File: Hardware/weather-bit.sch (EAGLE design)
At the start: 41 parts, among them J1 EDGE-80PTH-RA, J2 RJ11, J3 RJ11, U1 BME280

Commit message: Updated brd and sch file 3/28/2017
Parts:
- removed R2, R3: 4.7k, SparkFun-Resistors:4.7KOHM-0603-1/10W-1%
- added I2C: JUMPER-SMT_3_2-NC_TRACE_SILK, SparkFun-Jumpers:JUMPER-SMT_3_2-NC_TRACE_SILK
- added J8, J9: (no value), SparkFun-Connectors:CONN_04
- added R12, R13: 4.7k, SparkFun-Resistors:4.7KOHM-0603-1/10W-1%
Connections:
- removed net 14: J1.A17
- removed net 15: J1.A16
- new net N$4: I2C.3, R12.2
- new net N$8: I2C.1, R13.2
- new net RXI: J1.A17, J8.2
- new net TXO: J1.A16, J8.1
- net 3.3V: now also I2C.2, J8.4, J9.3; no longer R2.2, R3.2
- net GND: now also J8.3, J9.4
- net SCL: now also J9.1, R13.1; no longer R3.1
- net SDA: now also J9.2, R12.1; no longer R2.1
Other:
- note added: "I2C Port"
- note added: "RXI"
- note added: "Serial Port"
- note added: "TXO"

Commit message: updated board and sch files 3/29
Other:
- note added: "Mary West, based on Weather Shield design by Nathan Seidle"
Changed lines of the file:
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@@
 <text x="66.04" y="60.96" size="2.54" layer="97" font="vector">I2C Port </text>
 <wire x1="58.42" y1="68.58" x2="58.42" y2="0" width="0.1524" layer="97" style="longdash"/>
+<text x="167.64" y="10.16" size="1.778" layer="94">Mary West, based on Weather Shield design by Nathan Seidle</text>
 </plain>
 <instances>

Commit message: Adding Library Part Updated Brd File Updated Sch File 3/30/2017
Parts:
- removed I2C: JUMPER-SMT_3_2-NC_TRACE_SILK, SparkFun-Jumpers:JUMPER-SMT_3_2-NC_TRACE_SILK
- removed J1: EDGE-80PTH-RA, local_lib:EDGE-80PTH-RA
- removed R12, R13: 4.7k, SparkFun-Resistors:4.7KOHM-0603-1/10W-1%
- added U2: micro:bit, Micro_Bit_Parts:MICRO:BITLEDS_UP
- LOGO2: value SFE_LOGO_NAME_FLAME.1_INCH -> SFE_LOGO_NAME_FLAME.3_INCH; device SparkFun-Aesthetics:SFE_LOGO_NAME_FLAME.1_INCH -> SparkFun-Aesthetics:SFE_LOGO_NAME_FLAME.3_INCH
- LOGO3, LOGO4: value OSHW-LOGOS -> OSHW-LOGOL; device SparkFun-Aesthetics:OSHW-LOGOS -> SparkFun-Aesthetics:OSHW-LOGOL
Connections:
- removed net N$4: I2C.3, R12.2
- removed net N$8: I2C.1, R13.2
- net 10: now also U2.P10; no longer J1.A25
- net 11: now also U2.P11; no longer J1.A24
- net 13: now also U2.P13; no longer J1.A18
- net 3: now also U2.P3; no longer J1.A40
- net 3.3V: now also U2.3.3V; no longer I2C.2, J1.A10, J1.A11, J1.A12, J1.A13, J1.A14, J1.A9
- net 4: now also U2.P4; no longer J1.A35
- net 5: now also U2.P5; no longer J1.A34
- net 6: now also U2.P6; no longer J1.A33
- net 7: now also U2.P7; no longer J1.A32
- net 9: now also U2.P9; no longer J1.A26
- net GND: now also U2.GND; no longer J1.A1, J1.A2, J1.A3, J1.A4, J1.A5, J1.A6
- net RAIN: now also U2.P2; no longer J1.A19, J1.A20, J1.A21, J1.A22
- net RXI: now also U2.P14; no longer J1.A17
- net SCL: now also U2.P19; no longer J1.A8, R13.1
- net SDA: now also U2.P20; no longer J1.A7, R12.1
- net SOIL_DAT: now also U2.P0; no longer J1.A36, J1.A37, J1.A38, J1.A39
- net SOIL_PWR: now also U2.P16; no longer J1.A15
- net TEMP_DAT: now also U2.P12; no longer J1.A23
- net TXO: now also U2.P15; no longer J1.A16
- net WDIR: now also U2.P1; no longer J1.A28, J1.A29, J1.A30, J1.A31
- net WSPEED: now also U2.P8; no longer J1.A27

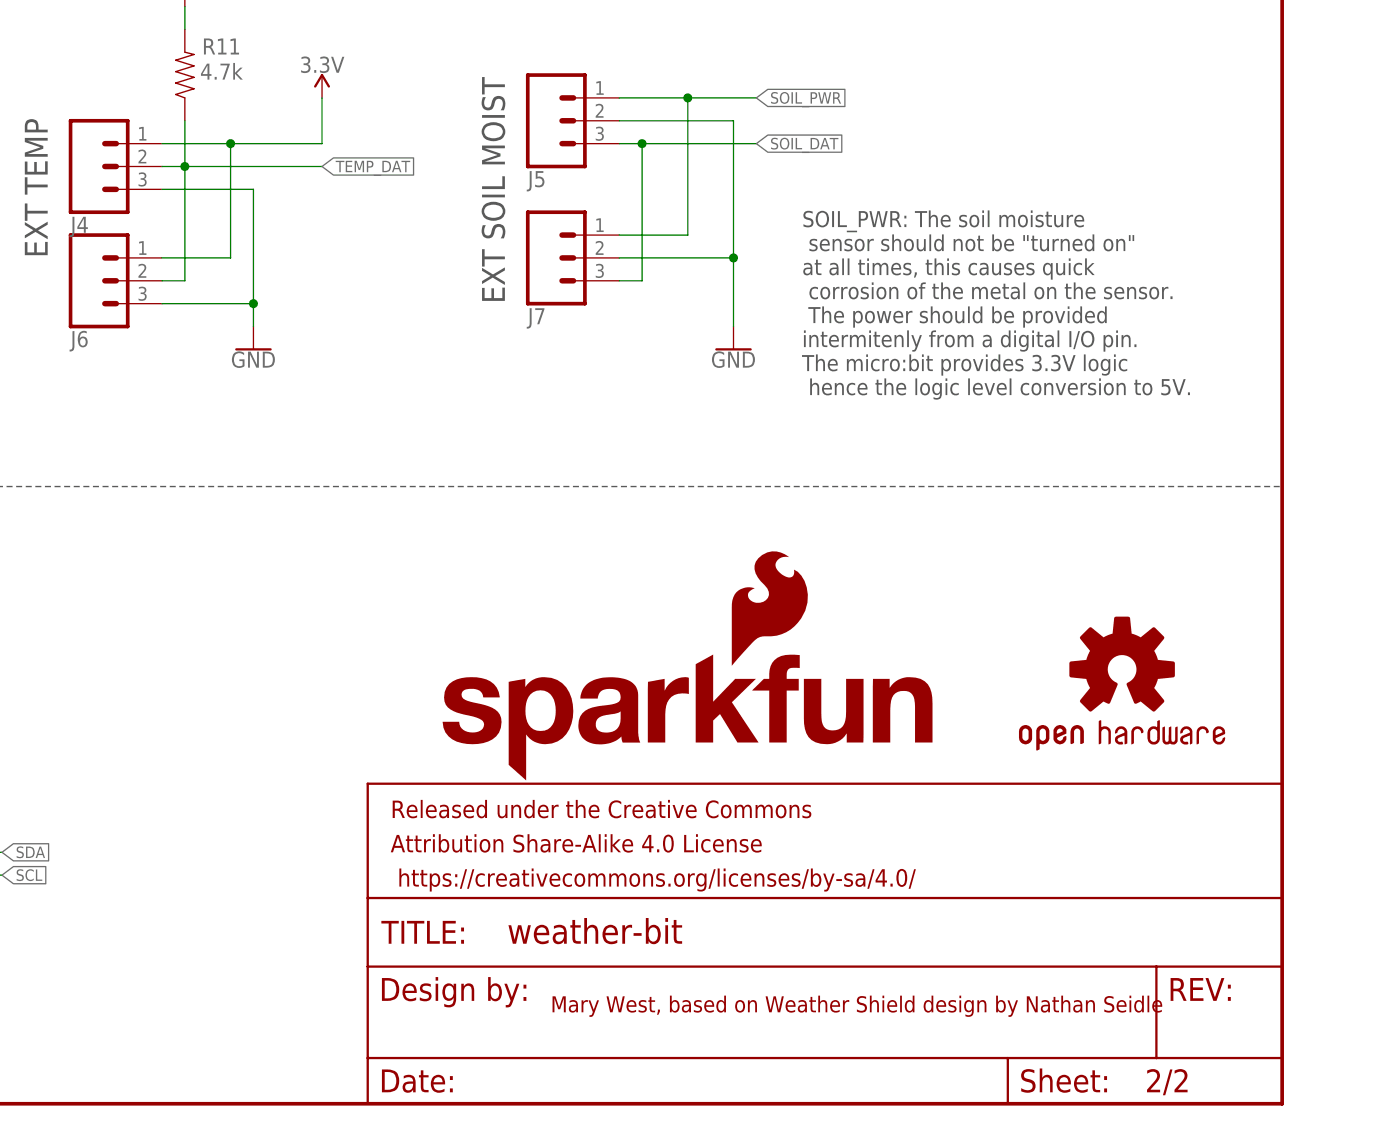
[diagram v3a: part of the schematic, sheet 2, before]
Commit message: Updated BRD and SCH files per Design Review 3/31
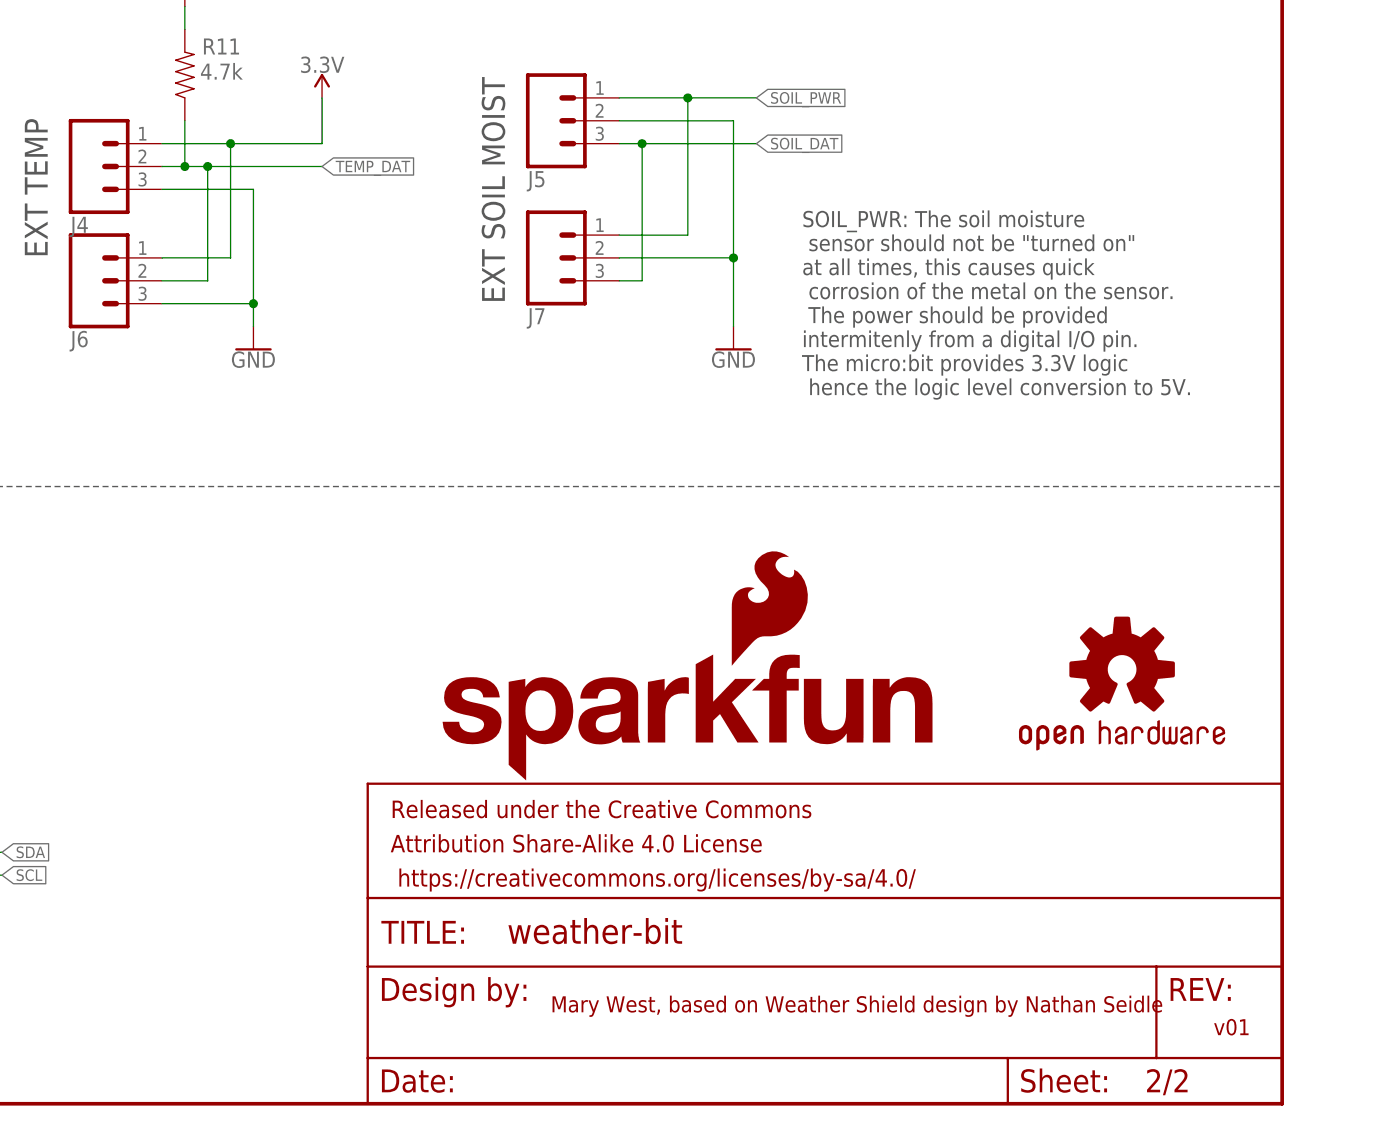
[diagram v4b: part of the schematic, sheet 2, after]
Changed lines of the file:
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@@
 The micro:bit provides 3.3V logic
  hence the logic level conversion to 5V. </text>
-<text x="111.76" y="93.98" size="2.54" layer="97" rot="R90">EXT TEMP</text>
-<text x="162.56" y="88.9" size="2.54" layer="97" rot="R90">EXT SOIL MOIST</text>
+<text x="111.76" y="93.98" size="2.54" layer="97" font="vector" rot="R90">EXT TEMP</text>
+<text x="162.56" y="88.9" size="2.54" layer="97" font="vector" rot="R90">EXT SOIL MOIST</text>
 <wire x1="96.52" y1="68.58" x2="248.92" y2="68.58" width="0.1524" layer="97" style="longdash"/>
 <wire x1="0" y1="134.62" x2="96.52" y2="134.62" width="0.1524" layer="97" style="longdash"/>
@@
 <wire x1="58.42" y1="68.58" x2="58.42" y2="0" width="0.1524" layer="97" style="longdash"/>
 <text x="167.64" y="10.16" size="1.778" layer="94">Mary West, based on Weather Shield design by Nathan Seidle</text>
+<text x="241.3" y="7.62" size="1.778" layer="94">v01</text>
 </plain>
 <instances>
@@
 <pinref part="R11" gate="G$1" pin="1"/>
 <wire x1="127" y1="109.22" x2="127" y2="104.14" width="0.1524" layer="91"/>
-<wire x1="127" y1="104.14" x2="127" y2="91.44" width="0.1524" layer="91"/>
+<junction x="127" y="104.14"/>
+<wire x1="127" y1="104.14" x2="129.54" y2="104.14" width="0.1524" layer="91"/>
+<label x="142.24" y="104.14" size="1.27" layer="95" xref="yes"/>
 <pinref part="J6" gate="J$1" pin="2"/>
-<wire x1="127" y1="91.44" x2="124.46" y2="91.44" width="0.1524" layer="91"/>
-<junction x="127" y="104.14"/>
-<wire x1="127" y1="104.14" x2="142.24" y2="104.14" width="0.1524" layer="91"/>
-<label x="142.24" y="104.14" size="1.27" layer="95" xref="yes"/>
-</segment>
-</net>
+<wire x1="129.54" y1="104.14" x2="142.24" y2="104.14" width="0.1524" layer="91"/>
+<wire x1="124.46" y1="91.44" x2="129.54" y2="91.44" width="0.1524" layer="91"/>
+<wire x1="129.54" y1="91.44" x2="129.54" y2="104.14" width="0.1524" layer="91"/>
+<junction x="129.54" y="104.14"/>
+</segment>
+</net>

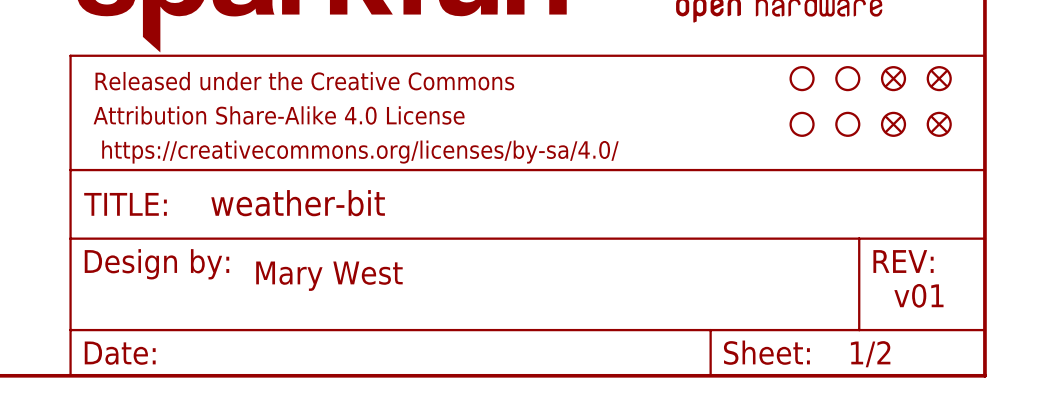
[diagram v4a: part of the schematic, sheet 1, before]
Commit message: Updated brd and sch files per QC Review
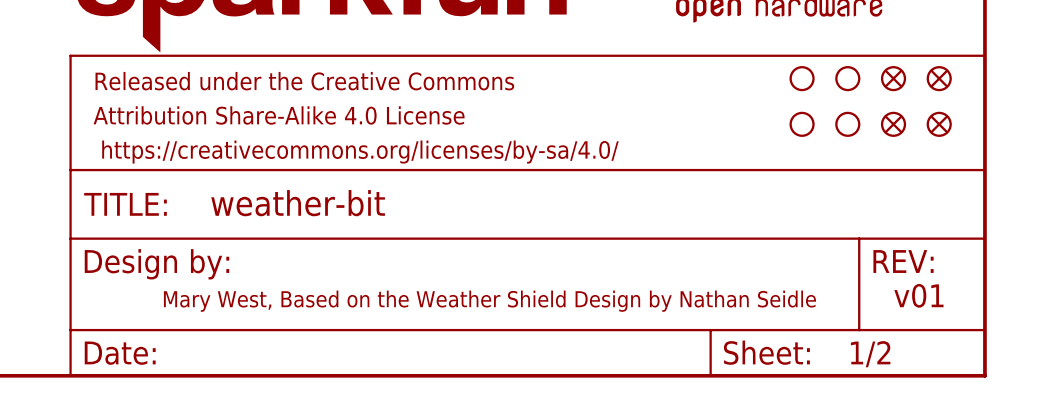
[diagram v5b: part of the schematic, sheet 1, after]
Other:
- note added: "Mary West, Based on the Weather Shield Design by Nathan Seidle"
- note removed: "Mary West"
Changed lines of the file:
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@@
 <text x="238.76" y="7.62" size="2.54" layer="94">v01</text>
 <text x="5.08" y="175.26" size="5.08" layer="97">CONNECTOR</text>
-<text x="167.64" y="10.16" size="2.54" layer="94" font="vector">Mary West </text>
 <text x="149.86" y="93.98" size="1.778" layer="97">20
 19
@@
 <text x="175.26" y="134.62" size="1.27" layer="97">TXO</text>
 <text x="175.26" y="132.08" size="1.27" layer="97">RXI</text>
+<text x="157.48" y="7.62" size="1.778" layer="94">Mary West, Based on the Weather Shield Design by Nathan Seidle</text>
 </plain>
 <instances>

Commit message: Updated BRD and SCH files per EDU
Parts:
- removed J8: (no value), SparkFun-Connectors:CONN_04
- removed LOGO4: OSHW-LOGOL, SparkFun-Aesthetics:OSHW-LOGOL
- added J1: (no value), SparkFun-Connectors:6_PIN_SERIAL_TARGETSILK
- J9: device SparkFun-Connectors:CONN_04 -> SparkFun-Connectors:CONN_041X04_NO_SILK
- LOGO1: value SFE_LOGO_NAME_FLAME.1_INCH -> SFE_LOGO_NAME_FLAME.2_INCH; device SparkFun-Aesthetics:SFE_LOGO_NAME_FLAME.1_INCH -> SparkFun-Aesthetics:SFE_LOGO_NAME_FLAME.2_INCH
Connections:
- net 3.3V: now also J1.VCC; no longer J8.4
- net GND: now also J1.CTS, J1.GND; no longer J8.3
- net RXI: now also J1.RXI; no longer J8.2
- net TXO: now also J1.TXO; no longer J8.1
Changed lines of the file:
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@@
 <part name="J7" library="SparkFun-Connectors" deviceset="CONN_03" device=""/>
 <part name="R11" library="SparkFun-Resistors" deviceset="4.7KOHM" device="-0603-1/10W-1%" value="4.7k"/>
-<part name="LOGO1" library="SparkFun-Aesthetics" deviceset="SFE_LOGO_NAME_FLAME" device=".1_INCH" value="SFE_LOGO_NAME_FLAME.1_INCH"/>
-<part name="LOGO4" library="SparkFun-Aesthetics" deviceset="OSHW-LOGO" device="L" value="OSHW-LOGOL"/>
+<part name="LOGO1" library="SparkFun-Aesthetics" deviceset="SFE_LOGO_NAME_FLAME" device=".2_INCH" value="SFE_LOGO_NAME_FLAME.2_INCH"/>
 <part name="GND15" library="SparkFun-PowerSymbols" deviceset="GND" device=""/>
 <part name="GND16" library="SparkFun-PowerSymbols" deviceset="GND" device=""/>
@@
 <part name="SUPPLY9" library="SparkFun-PowerSymbols" deviceset="3.3V" device=""/>
 <part name="SUPPLY10" library="SparkFun-PowerSymbols" deviceset="3.3V" device=""/>
-<part name="J8" library="SparkFun-Connectors" deviceset="CONN_04" device=""/>
-<part name="J9" library="SparkFun-Connectors" deviceset="CONN_04" device=""/>
+<part name="J9" library="SparkFun-Connectors" deviceset="CONN_04" device="1X04_NO_SILK"/>
 <part name="SUPPLY11" library="SparkFun-PowerSymbols" deviceset="3.3V" device=""/>
 <part name="GND2" library="SparkFun-PowerSymbols" deviceset="GND" device=""/>
@@
 <part name="SUPPLY8" library="SparkFun-PowerSymbols" deviceset="3.3V" device=""/>
 <part name="GND4" library="SparkFun-PowerSymbols" deviceset="GND" device=""/>
+<part name="J1" library="SparkFun-Connectors" deviceset="6_PIN_SERIAL_TARGET" device="SILK"/>
 </parts>
 <sheets>
@@
 </instance>
 <instance part="LOGO1" gate="G$1" x="154.94" y="35.56"/>
-<instance part="LOGO4" gate="G$1" x="231.14" y="48.26"/>
 <instance part="GND15" gate="1" x="134.62" y="83.82"/>
 <instance part="GND16" gate="1" x="187.96" y="83.82"/>
@@
 <instance part="SUPPLY9" gate="G$1" x="166.37" y="179.324"/>
 <instance part="SUPPLY10" gate="G$1" x="173.99" y="179.324"/>
-<instance part="J8" gate="G$1" x="20.32" y="38.1"/>
 <instance part="J9" gate="G$1" x="78.74" y="27.94"/>
-<instance part="SUPPLY11" gate="G$1" x="33.02" y="48.26"/>
-<instance part="GND2" gate="1" x="33.02" y="22.86"/>
+<instance part="SUPPLY11" gate="G$1" x="33.02" y="53.34"/>
+<instance part="GND2" gate="1" x="27.94" y="25.4"/>
 <instance part="SUPPLY12" gate="G$1" x="88.9" y="40.64"/>
 <instance part="GND3" gate="1" x="91.44" y="15.24"/>
+<instance part="J1" gate="G$1" x="17.78" y="40.64"/>
 </instances>
 <busses>
@@
 </segment>
 <segment>
-<pinref part="J8" gate="G$1" pin="3"/>
-<wire x1="25.4" y1="40.64" x2="33.02" y2="40.64" width="0.1524" layer="91"/>
-<wire x1="33.02" y1="40.64" x2="33.02" y2="25.4" width="0.1524" layer="91"/>
-<pinref part="GND2" gate="1" pin="GND"/>
-</segment>
-<segment>
 <pinref part="J9" gate="G$1" pin="4"/>
 <wire x1="83.82" y1="33.02" x2="91.44" y2="33.02" width="0.1524" layer="91"/>
 <wire x1="91.44" y1="33.02" x2="91.44" y2="17.78" width="0.1524" layer="91"/>
 <pinref part="GND3" gate="1" pin="GND"/>
+</segment>
+<segment>
+<pinref part="J1" gate="G$1" pin="GND"/>
+<wire x1="22.86" y1="48.26" x2="27.94" y2="48.26" width="0.1524" layer="91"/>
+<wire x1="27.94" y1="48.26" x2="27.94" y2="45.72" width="0.1524" layer="91"/>
+<pinref part="GND2" gate="1" pin="GND"/>
+<pinref part="J1" gate="G$1" pin="CTS"/>
+<wire x1="27.94" y1="45.72" x2="27.94" y2="27.94" width="0.1524" layer="91"/>
+<wire x1="22.86" y1="45.72" x2="27.94" y2="45.72" width="0.1524" layer="91"/>
+<junction x="27.94" y="45.72"/>
 </segment>
 </net>
@@
 </segment>
 <segment>
-<pinref part="J8" gate="G$1" pin="4"/>
-<wire x1="25.4" y1="43.18" x2="33.02" y2="43.18" width="0.1524" layer="91"/>
-<wire x1="33.02" y1="43.18" x2="33.02" y2="48.26" width="0.1524" layer="91"/>
-<pinref part="SUPPLY11" gate="G$1" pin="3.3V"/>
-</segment>
-<segment>
 <pinref part="J9" gate="G$1" pin="3"/>
 <wire x1="83.82" y1="30.48" x2="88.9" y2="30.48" width="0.1524" layer="91"/>
 <wire x1="88.9" y1="30.48" x2="88.9" y2="40.64" width="0.1524" layer="91"/>
 <pinref part="SUPPLY12" gate="G$1" pin="3.3V"/>
+</segment>
+<segment>
+<pinref part="J1" gate="G$1" pin="VCC"/>
+<wire x1="22.86" y1="43.18" x2="33.02" y2="43.18" width="0.1524" layer="91"/>
+<pinref part="SUPPLY11" gate="G$1" pin="3.3V"/>
+<wire x1="33.02" y1="43.18" x2="33.02" y2="53.34" width="0.1524" layer="91"/>
 </segment>
 </net>
@@
 </segment>
 </net>
+<net name="TXO" class="0">
+<segment>
+<pinref part="J1" gate="G$1" pin="TXO"/>
+<wire x1="22.86" y1="40.64" x2="35.56" y2="40.64" width="0.1524" layer="91"/>
+<label x="35.56" y="40.64" size="1.27" layer="95" font="vector" xref="yes"/>
+</segment>
+</net>
 <net name="RXI" class="0">
 <segment>
-<pinref part="J8" gate="G$1" pin="2"/>
-<wire x1="25.4" y1="38.1" x2="38.1" y2="38.1" width="0.1524" layer="91"/>
-<label x="38.1" y="38.1" size="1.27" layer="95" xref="yes"/>
-</segment>
-</net>
-<net name="TXO" class="0">
-<segment>
-<pinref part="J8" gate="G$1" pin="1"/>
-<wire x1="25.4" y1="35.56" x2="38.1" y2="35.56" width="0.1524" layer="91"/>
-<label x="38.1" y="35.56" size="1.27" layer="95" xref="yes"/>
-</segment>
-</net>
+<pinref part="J1" gate="G$1" pin="RXI"/>
+<wire x1="22.86" y1="38.1" x2="35.56" y2="38.1" width="0.1524" layer="91"/>
+<label x="35.56" y="38.1" size="1.27" layer="95" font="vector" xref="yes"/>
+</segment>
+</net>

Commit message: Updated BRD and SCH files per EDU
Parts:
- removed LOGO1: SFE_LOGO_NAME_FLAME.2_INCH, SparkFun-Aesthetics:SFE_LOGO_NAME_FLAME.2_INCH
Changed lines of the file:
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@@
 <part name="J7" library="SparkFun-Connectors" deviceset="CONN_03" device=""/>
 <part name="R11" library="SparkFun-Resistors" deviceset="4.7KOHM" device="-0603-1/10W-1%" value="4.7k"/>
-<part name="LOGO1" library="SparkFun-Aesthetics" deviceset="SFE_LOGO_NAME_FLAME" device=".2_INCH" value="SFE_LOGO_NAME_FLAME.2_INCH"/>
 <part name="GND15" library="SparkFun-PowerSymbols" deviceset="GND" device=""/>
 <part name="GND16" library="SparkFun-PowerSymbols" deviceset="GND" device=""/>
@@
 <attribute name="VALUE" x="131.064" y="113.792" size="1.778" layer="96" font="vector" rot="R180" align="top-center"/>
 </instance>
-<instance part="LOGO1" gate="G$1" x="154.94" y="35.56"/>
 <instance part="GND15" gate="1" x="134.62" y="83.82"/>
 <instance part="GND16" gate="1" x="187.96" y="83.82"/>

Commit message: replacing proportional font back to vector font
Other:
- note added: "SOIL_PWR: The soil moisture sensor should not be "turned on" at all times, this causes quick corrosion of the metal on the sensor. The power should be provided intermitenly from a digital I/O pin."
- note removed: "SOIL_PWR: The soil moisture sensor should not be "turned on" at all times, this causes quick corrosion of the metal on the sensor. The power should be provided intermitenly from a digital I/O pin. The micro:bit provides 3.3V logic hence the logic level conversion to 5V."
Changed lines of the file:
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@@
  corrosion of the metal on the sensor.
  The power should be provided
-intermitenly from a digital I/O pin.
-The micro:bit provides 3.3V logic
- hence the logic level conversion to 5V. </text>
+intermitenly from a digital I/O pin. </text>
 <text x="111.76" y="93.98" size="2.54" layer="97" font="vector" rot="R90">EXT TEMP</text>
 <text x="162.56" y="88.9" size="2.54" layer="97" font="vector" rot="R90">EXT SOIL MOIST</text>
